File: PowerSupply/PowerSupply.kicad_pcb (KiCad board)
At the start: 2 copper layers, 13 parts, among them J1 POWER, J2 CONTROL, J3 LASER, U0 AL8861Y-13

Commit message: Basic pcb layout
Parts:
- moved H4 47.7 mm to (167.0, 66.0)
- moved H1 42.6 mm to (129.0, 66.0)
- moved H2 32.2 mm to (129.0, 95.0)
- moved L1 25.3 mm to (147.1, 76.0), turned to 0 degrees
- moved H3 23.9 mm to (167.0, 95.0)
- moved J2 9.40 mm to (149.9, 88.9), turned to 0 degrees
- moved J3 7.88 mm to (149.9, 81.3)
- moved J1 6.39 mm to (149.9, 73.7)
- moved D1 4.49 mm to (135.0, 79.0)
- moved C1 1.95 mm to (143.0, 78.0), turned to 180 degrees
- moved R2 1.74 mm to (138.0, 86.0)
- moved U0 0.72 mm to (139.7, 82.0)
- moved R1 0.27 mm to (144.8, 82.0)
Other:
- board outline added: 46 x 37 mm

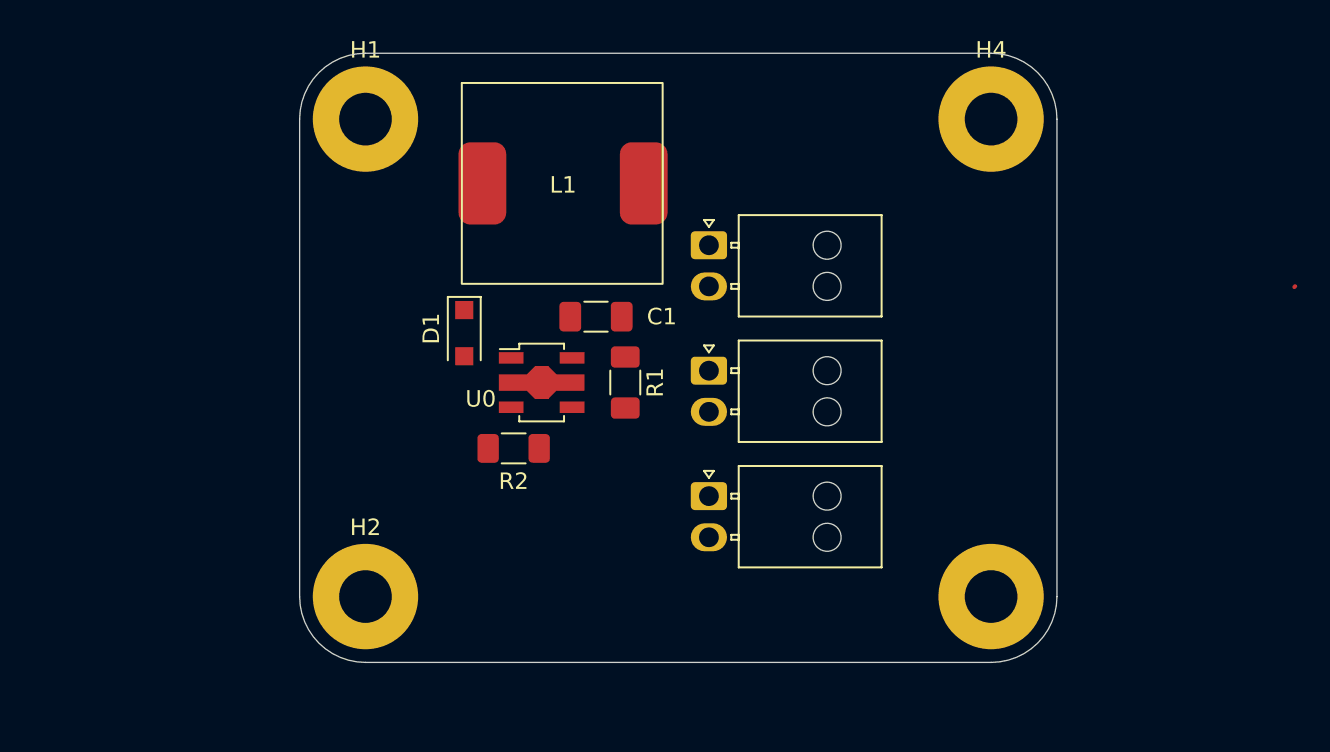
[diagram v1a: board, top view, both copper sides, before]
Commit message: Review: 1st round - Schema & PCB - General modifications
All comments in design files, more on chat
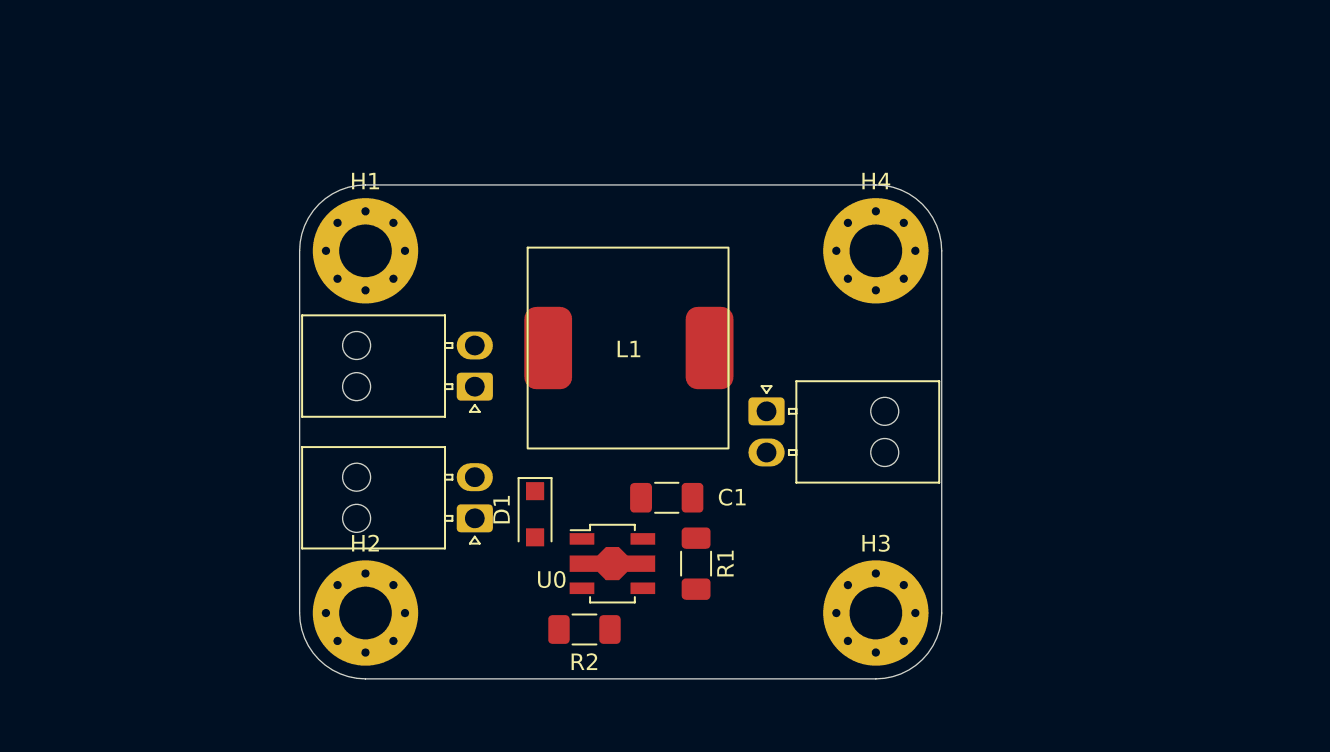
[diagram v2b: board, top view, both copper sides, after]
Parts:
- H1, H2, H3, H4: footprint MountingHole:MountingHole_3.2mm_M3_Pad -> MountingHole:MountingHole_3.2mm_M3_Pad_Via
- moved J1 16.6 mm to (135.6, 82.2), turned to 180 degrees
- moved J2 14.3 mm to (135.6, 90.2), turned to 180 degrees
- moved C1 11.8 mm to (147.3, 89.0)
- moved D1 11.8 mm to (139.3, 90.0)
- moved R1 11.8 mm to (149.1, 93.0)
- moved R2 11.8 mm to (142.3, 97.0)
- moved U0 11.8 mm to (144.0, 93.0)
- moved L1 10.8 mm to (151.1, 86.0)
- moved H4 10.6 mm to (160.0, 74.0)
- moved H1 8.00 mm to (129.0, 74.0)
- moved H3 7.07 mm to (160.0, 96.0)
- moved J3 4.28 mm to (153.4, 83.8)
- moved H2 1.00 mm to (129.0, 96.0)
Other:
- board size 46 x 37 mm -> 39 x 30 mm
- board text added: "Doporučuji skrýt labels u mounting holes"
- board text added: "Ideální je všemu přiřadit 3D modely (pro molex najdete step na Mouseru, je potřeba jim změnit pár nastavení)"
- board text added: "Kolik prostoru potřebujete okolo součástek většinou poznáte podle vestvy countryard, ktera by mela označovat velikost komponenty, ideálně pak i podle 3D modelu desky, ale to musíte mít vsude modely (což je pracné) ale durazně to doporucuji"
- board text added: "TIP: třeba u cívky dost možná nenajdete stejný model, vemte jiný a přímo v kicadu jej trochu nascalujte a zarovnejte aby odpovídal vasi civce, aby jste ji nemusel modelovat nebo jinak shanet"
- board text added: "Titulní blok"
- board text added: "V průběhu routování nezapoměnte na DRC (Design rule check) horní paněl vedle importu ze schematu"

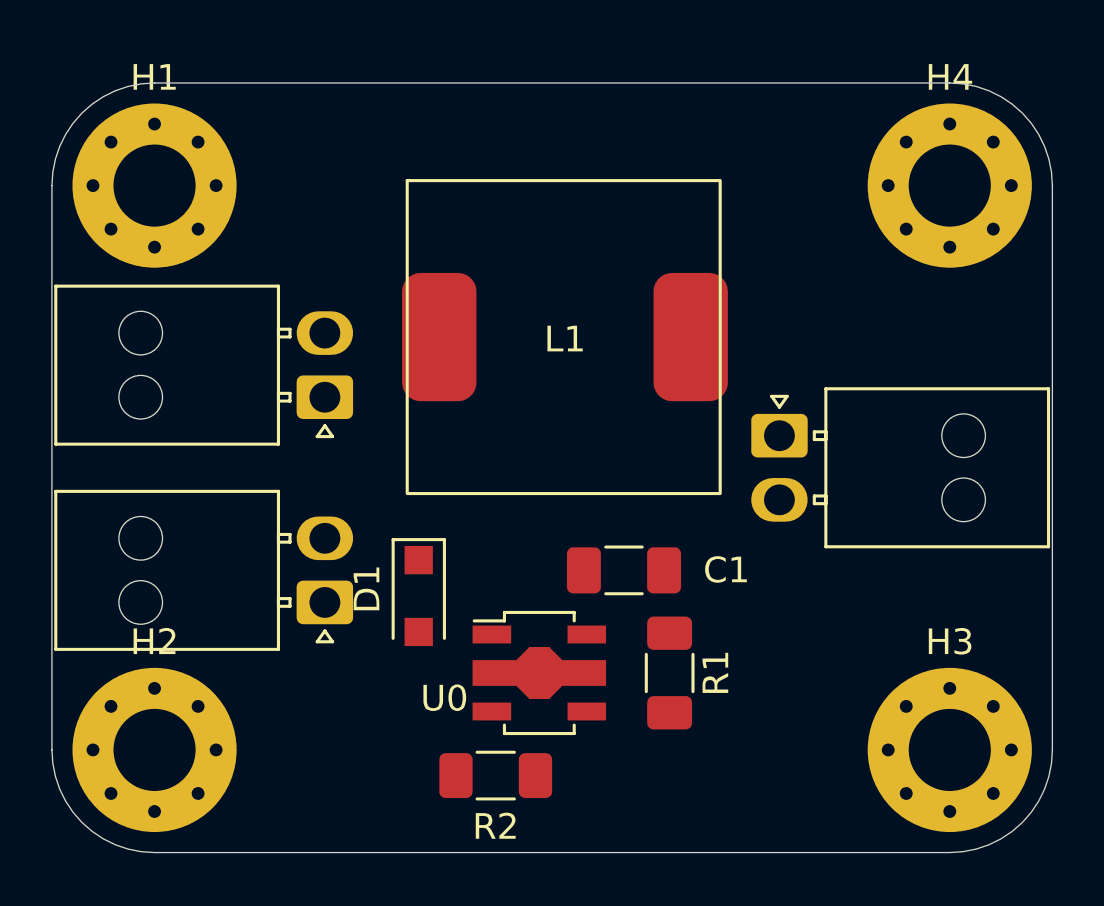
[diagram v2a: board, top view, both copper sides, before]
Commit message: Resolved first review, Routing
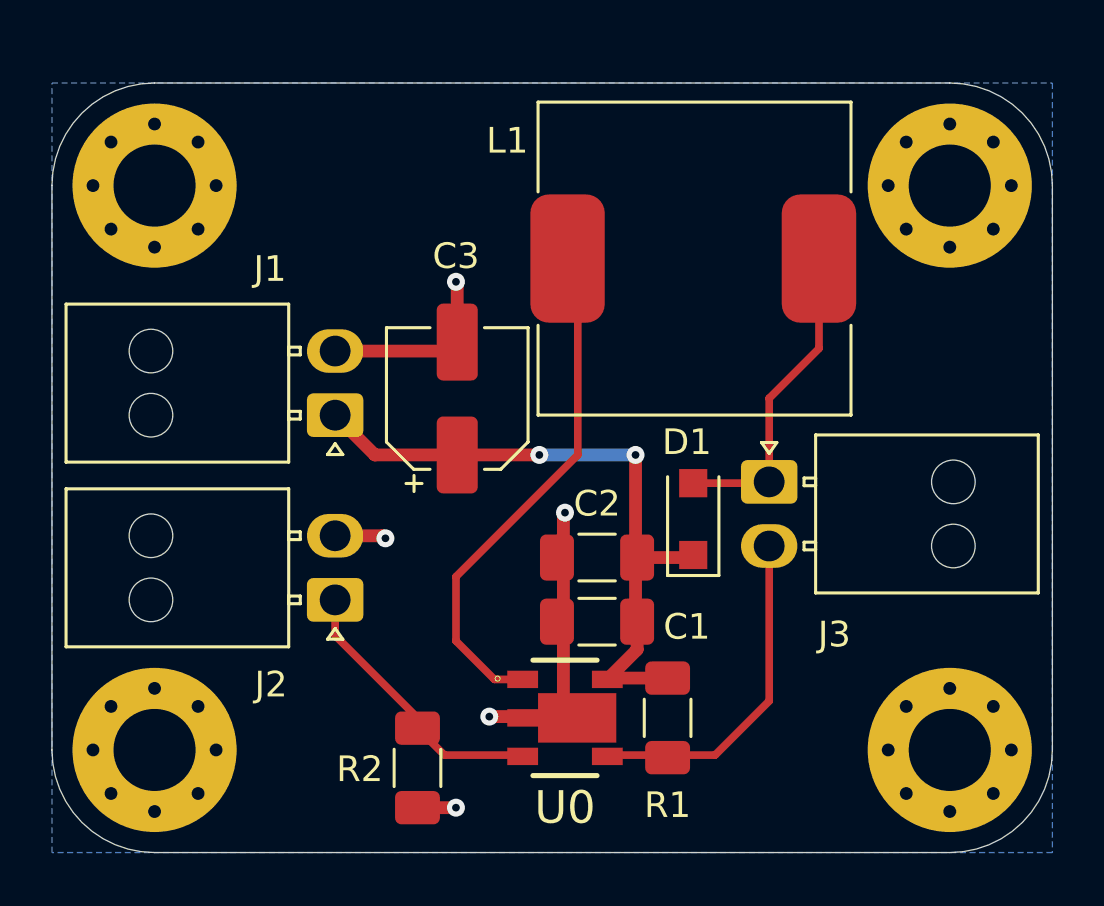
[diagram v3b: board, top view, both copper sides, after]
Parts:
- added C2: 100nF, Capacitor_SMD:C_1206_3216Metric_Pad1.33x1.80mm_HandSolder, F.Cu at (146.2, 88.5)
- added C3: 100uF, Capacitor_SMD:CP_Elec_5x5.3, F.Cu at (140.8, 82.3)
- H1, H2, H3, H4: value MountingHole_Pad -> M3
- J2: value CONTROL -> VSET
- U0: footprint Package_TO_SOT_SMD:SOT-89-5 -> SamacSys_Parts:SOT89-5
- moved L1 16.8 mm to (143.9, 70.7), turned to 180 degrees
- moved D1 11.1 mm to (150.0, 87.0), turned to 90 degrees
- moved R2 3.06 mm to (139.2, 96.7), turned to -90 degrees
- moved C1 2.26 mm to (146.2, 91.0)
- moved U0 2.02 mm to (145.0, 94.8), turned to -90 degrees
- moved J3 1.84 mm to (153.0, 85.5)
- moved R1 1.75 mm to (149.0, 94.8)
- moved J1 0.81 mm to (136.0, 83.0)
- moved J2 0.41 mm to (136.0, 90.2)
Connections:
- net Net-(J2-Pad1) renamed /VSET
- net Net-(J3-Pad2) renamed /ISENSE
- D1 pad 2: Net-(D1-Pad2) -> Net-(J3-Pad1)
- L1 pad 1: Net-(J3-Pad1) -> Net-(U0-Pad1)
- L1 pad 2: Net-(D1-Pad2) -> Net-(J3-Pad1)
- U0 pad 1: Net-(D1-Pad2) -> Net-(U0-Pad1)
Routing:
- net +5V: track 0.00 -> 26.0 mm, vias 0 -> 2
- net Net-(U0-Pad1): track 0.00 -> 20.3 mm
- net GND: track 0.00 -> 20.2 mm, vias 0 -> 5
- net /ISENSE: track 0.00 -> 13.2 mm
- net Net-(J3-Pad1): track 0.00 -> 12.2 mm
- net /VSET: track 0.00 -> 10.9 mm
- added copper zone on B.Cu, net GND
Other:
- board text removed: "Doporučuji skrýt labels u mounting holes"
- board text removed: "Ideální je všemu přiřadit 3D modely (pro molex najdete step na Mouseru, je potřeba jim změnit pár nastavení)"
- board text removed: "Kolik prostoru potřebujete okolo součástek většinou poznáte podle vestvy countryard, ktera by mela označovat velikost komponenty, ideálně pak i podle 3D modelu desky, ale to musíte mít vsude modely (což je pracné) ale durazně to doporucuji"
- board text removed: "TIP: třeba u cívky dost možná nenajdete stejný model, vemte jiný a přímo v kicadu jej trochu nascalujte a zarovnejte aby odpovídal vasi civce, aby jste ji nemusel modelovat nebo jinak shanet"
- board text removed: "V průběhu routování nezapoměnte na DRC (Design rule check) horní paněl vedle importu ze schematu"

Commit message: Review: 2st round - PCB - General routing (planes, vias, pads routing)
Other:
- board text added: "Ideální je mít GND plane na obou vrstvách Stačí v nastaveí plane vybrat i druhou vrstvu"
- board text added: "Ideální je na desku přidat i popisek (vrstva silkscreen) s datem, verzí, o co se jedná a kdo je autor"
- board text added: "Neni nutne mit extra tenke cesty, klidně by zde vsiude mohlo být 0.5mm"
- board text added: "Pokud je to možné použijte standardní footprint Tento konkrétní v knihovnách kicadu je: Doporučuji minimálně stahovat, radši si to nakreslete sám pak neskončíte s nekvalitními footprinty Tento zrovna není ideální, z knihovny: Package_TO_SOT_SMD:SOT-89-5"
- board text added: "Při updatu PCB ze schematu jsou nejake chyby stejne tak ERC ukazuje varování Ještě jednou poznamenávám že než mi to pošlete na review meli by vsechny kontroly ukazovat 0 chyba 0 varování Konkrétně ERC, update PCB ze schematu, DRC"
- board text added: "Spínací cesta by měla být co nejkratší kvůli rušení a zpětné vazbě, vy ji máte nejdelší Doporučuji shlédnout: https://www.youtube.com/watch?v=AmfLhT5SntE Je to obdobné reší spínaný regulátor, což je téměř identické. Tento konkrétné obvod neumoznuje uplne ideální zapojení nicméně slo by to o hodně zlepsit"
- board text added: "Tento prokov je zbytečný Prokovení je způsobeno už uchycením THT součástky zde V případě GND plochy na obou stranách by neměl už vůbec cenu Má cenu ovšem prokovit dvě GND plochy mezi sebou (vis stitching) Stitching je vhodný pro návratové proudy a tepelnou distribuci Plugin: https://github.com/jsreynaud/kicad-action-scripts nebo https://github.com/weirdgyn/viastitching"
- board text added: "U konektoru by měl být popisek k čemu jsou a jaké je jejih polarita Usnadní to ozivovaní a použivani"
- board text added: "Z plosek se snazte jit pokud mozno kolmo na jejich tvar Ma to zase vliv na ruseni a u desek s uzsimi cesty i na jejich vyrobitelnost"
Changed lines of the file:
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@@
     )
   )
+  (gr_line (start 141.8 101.85) (end 160.45 101.45) (layer "Cmts.User") (width 0.1))
+  (gr_line (start 142.25 93.3) (end 143.35 93.3) (layer "Cmts.User") (width 0.1))
+  (gr_circle (center 144.75 94.7) (end 147.9 94.65) (layer "Cmts.User") (width 0.1) (fill none))
+  (gr_line (start 123.95 81) (end 106.95 81.7) (layer "Cmts.User") (width 0.1))
+  (gr_line (start 186.2 168.55) (end 170.55 147.65) (layer "Cmts.User") (width 0.1))
+  (gr_line (start 155.05 80.5) (end 155.35 81.05) (layer "Cmts.User") (width 0.1))
+  (gr_line (start 246.8 136.05) (end 272.9 132.1) (layer "Cmts.User") (width 0.1))
+  (gr_line (start 150.9 96.25) (end 152.95 94.1) (layer "Cmts.User") (width 0.1))
+  (gr_line (start 155.05 80.5) (end 155.6 80.25) (layer "Cmts.User") (width 0.1))
+  (gr_circle (center 138 87.7) (end 138.7 87.6) (layer "Cmts.User") (width 0.1) (fill none))
+  (gr_line (start 140.8 91.5) (end 142.25 93.3) (layer "Cmts.User") (width 0.1))
+  (gr_line (start 144.85 97.85) (end 146.25 103.05) (layer "Cmts.User") (width 0.1))
+  (gr_line (start 145.55 84.4) (end 140.75 89.1) (layer "Cmts.User") (width 0.1))
+  (gr_line (start 312.6 29) (end 247.3 136.55) (layer "Cmts.User") (width 0.1))
+  (gr_line (start 186.2 168.35) (end 168.8 186.4) (layer "Cmts.User") (width 0.1))
+  (gr_line (start 167.1 69.3) (end 164.05 69.95) (layer "Cmts.User") (width 0.1))
+  (gr_line (start 140.75 89.1) (end 140.8 91.5) (layer "Cmts.User") (width 0.1))
+  (gr_line (start 153 82.2) (end 154.9 80.25) (layer "Cmts.User") (width 0.1))
+  (gr_line (start 247.3 136.55) (end 248 116.9) (layer "Cmts.User") (width 0.1))
+  (gr_line (start 146.7 96.3) (end 150.9 96.25) (layer "Cmts.User") (width 0.1))
+  (gr_line (start 152.95 94.1) (end 153 82.2) (layer "Cmts.User") (width 0.1))
+  (gr_line (start 4.85 156.95) (end 186.2 168.55) (layer "Cmts.User") (width 0.1))
+  (gr_circle (center 139.05 95) (end 140.6 95.05) (layer "Cmts.User") (width 0.1) (fill none))
+  (gr_line (start 147.651249 93.2) (end 169.3 95.9) (layer "Cmts.User") (width 0.1))
+  (gr_line (start 137.25 85.25) (end 123.95 81) (layer "Cmts.User") (width 0.1))
+  (gr_circle (center 135.9 87.75) (end 137.15 87.65) (layer "Cmts.User") (width 0.1) (fill none))
+  (gr_line (start 119.3 83.65) (end 134.65 87.4) (layer "Cmts.User") (width 0.1))
+  (gr_line (start 154.9 76.75) (end 145.3 76.75) (layer "Cmts.User") (width 0.1))
+  (gr_circle (center 223.3 168.65) (end 259.7 168.3) (layer "Cmts.User") (width 0.1) (fill none))
+  (gr_line (start 160.45 101.45) (end 169.4 95.9) (layer "Cmts.User") (width 0.1))
+  (gr_line (start 137.25 85.25) (end 137.95 86.95) (layer "Cmts.User") (width 0.1))
+  (gr_line (start 169.05 83.55) (end 155.05 80.5) (layer "Cmts.User") (width 0.1))
+  (gr_line (start 139.3 96.5) (end 141.8 101.85) (layer "Cmts.User") (width 0.1))
+  (gr_line (start 154.9 80.25) (end 154.9 76.75) (layer "Cmts.User") (width 0.1))
+  (gr_circle (center 146.65 93.2) (end 147.65 93.25) (layer "Cmts.User") (width 0.1) (fill none))
+  (gr_line (start 145.3 76.75) (end 145.55 84.4) (layer "Cmts.User") (width 0.1))
   (gr_line (start 125 74) (end 125 96) (layer "Edge.Cuts") (width 0.05))
   (gr_arc (start 164 96) (mid 162.828427 98.828427) (end 160 100) (layer "Edge.Cuts") (width 0.05))
@@
   (gr_line (start 129 100) (end 160 100) (layer "Edge.Cuts") (width 0.05))
   (gr_arc (start 129 100) (mid 126.171573 98.828427) (end 125 96) (layer "Edge.Cuts") (width 0.05))
-  (gr_text "Titulní blok" (at 227 158) (layer "Cmts.User")
+  (gr_text "Tento prokov je zbytečný\nProkovení je způsobeno už uchycením THT součástky zde\nV případě GND plochy na obou stranách by neměl už vůbec cenu\nMá cenu ovšem prokovit dvě GND plochy mezi sebou (vis stitching)\nStitching je vhodný pro návratové proudy a tepelnou distribuci\nPlugin: https://github.com/jsreynaud/kicad-action-scripts\nnebo https://github.com/weirdgyn/viastitching\n" (at 95.9 86.75) (layer "Cmts.User")
+    (effects (font (size 1 1) (thickness 0.15)))
+  )
+  (gr_text "Ideální je mít GND plane na obou vrstvách\nStačí v nastaveí plane vybrat i druhou vrstvu" (at 184.8 69.9) (layer "Cmts.User")
+    (effects (font (size 1 1) (thickness 0.15)))
+  )
+  (gr_text "Při updatu PCB ze schematu jsou nejake chyby stejne tak ERC ukazuje varování\nJeště jednou poznamenávám že než mi to pošlete na review meli by vsechny kontroly ukazovat 0 chyba 0 varování\nKonkrétně ERC, update PCB ze schematu, DRC" (at 183.3 61.05) (layer "Cmts.User")
+    (effects (font (size 1 1) (thickness 0.15)))
+  )
+  (gr_text "Z plosek se snazte jit pokud mozno kolmo na jejich tvar\nMa to zase vliv na ruseni a u desek s uzsimi cesty i na jejich vyrobitelnost" (at 196.5 97.85) (layer "Cmts.User")
+    (effects (font (size 1 1) (thickness 0.15)))
+  )
+  (gr_text "U konektoru by měl být popisek k čemu jsou a jaké je jejih polarita\nUsnadní to ozivovaní a použivani" (at 100.35 61) (layer "Cmts.User")
+    (effects (font (size 1 1) (thickness 0.15)))
+  )
+  (gr_text "Neni nutne mit extra tenke cesty, klidně by zde vsiude mohlo být 0.5mm" (at 102.5 65.4) (layer "Cmts.User")
+    (effects (font (size 1 1) (thickness 0.15)))
+  )
+  (gr_text "Pokud je to možné použijte standardní footprint\nTento konkrétní v knihovnách kicadu je: \nDoporučuji minimálně stahovat, radši si to nakreslete sám pak neskončíte s nekvalitními footprinty\nTento zrovna není ideální, z knihovny: Package_TO_SOT_SMD:SOT-89-5" (at 147.05 106.8) (layer "Cmts.User")
+    (effects (font (size 1 1) (thickness 0.15)))
+  )
+  (gr_text "Ideální je na desku přidat i popisek (vrstva silkscreen) s datem, verzí, o co se jedná a kdo je autor" (at 136.05 51.25) (layer "Cmts.User")
+    (effects (font (size 1 1) (thickness 0.15)))
+  )
+  (gr_text "Spínací cesta by měla být co nejkratší kvůli rušení a zpětné vazbě, vy ji máte nejdelší\nDoporučuji shlédnout: https://www.youtube.com/watch?v=AmfLhT5SntE\nJe to obdobné reší spínaný regulátor, což je téměř identické.\nTento konkrétné obvod neumoznuje uplne ideální zapojení nicméně slo by to o hodně zlepsit" (at 203.45 84.65) (layer "Cmts.User")
+    (effects (font (size 1 1) (thickness 0.15)))
+  )
+  (gr_text "Titulní blok" (at 222.65 169.75) (layer "Cmts.User")
     (effects (font (size 5 5) (thickness 0.5)))
   )
